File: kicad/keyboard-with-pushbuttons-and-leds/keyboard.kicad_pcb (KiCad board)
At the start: 2 copper layers, 138 parts, among them J1 CONN_01X02_MALE, J2 CONN_01X02_MALE, J3 CONN_01X04_MALE, J4 CONN_02X20, SW1 SW_Push, SW10 SW_Push, SW11 SW_Push, SW12 SW_Push, SW13 SW_Push, SW14 SW_Push, SW15 SW_Push, SW16 SW_Push, SW17 SW_Push, SW18 SW_Push, SW19 SW_Push, SW2 SW_Push, SW20 SW_Push, SW21 SW_Push, SW22 SW_Push, SW23 SW_Push, SW24 SW_Push, SW25 SW_Push, SW26 SW_Push, SW27 SW_Push, SW28 SW_Push, SW29 SW_Push, SW3 SW_Push, SW30 SW_Push, SW31 SW_Push, SW32 SW_Push, SW33 SW_Push, SW34 SW_Push, SW35 SW_Push, SW36 SW_Push, SW37 SW_Push, SW38 SW_Push, SW39 SW_Push, SW4 SW_Push, SW40 SW_Push, SW41 SW_Push, SW42 SW_Push, SW43 SW_Push, SW44 SW_Push, SW5 SW_Push, SW6 SW_Push, SW7 SW_Push, SW8 SW_Push, SW9 SW_Push

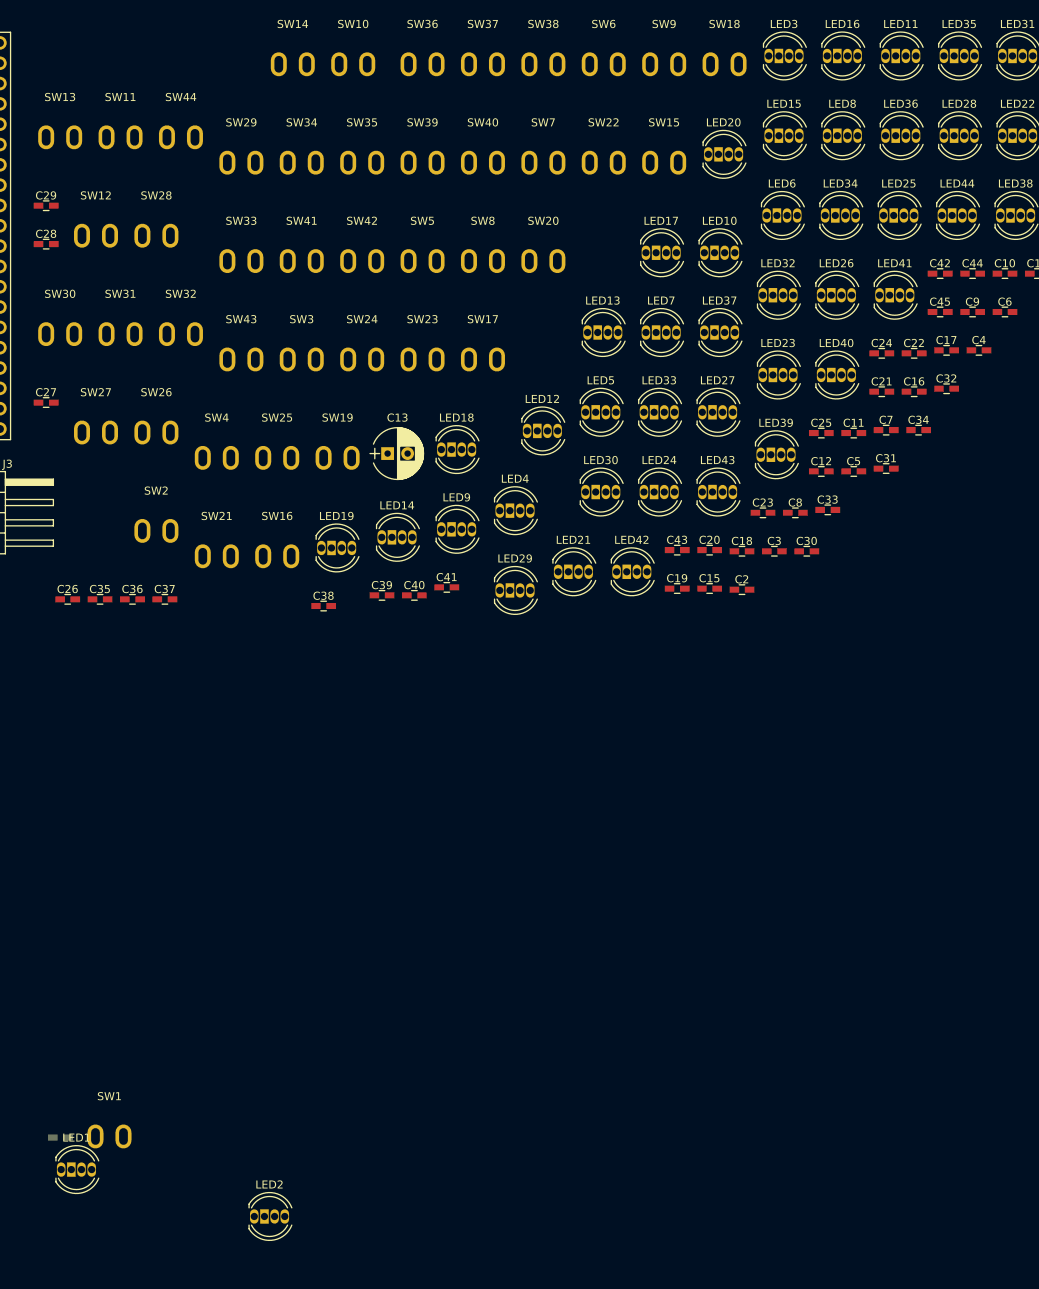
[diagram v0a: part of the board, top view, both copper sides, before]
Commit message: start creating a pattern
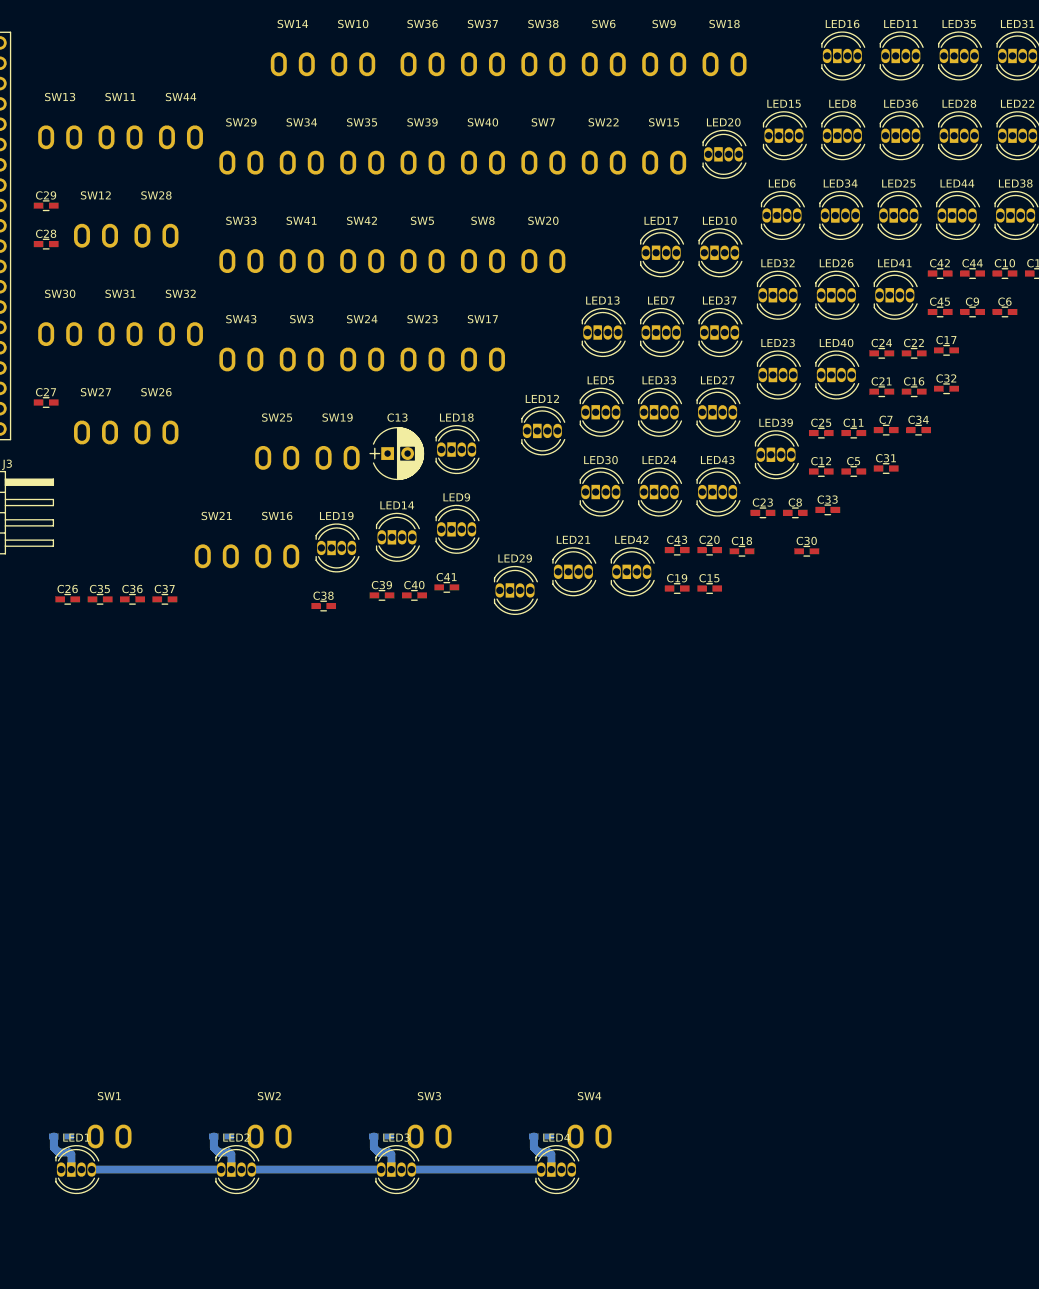
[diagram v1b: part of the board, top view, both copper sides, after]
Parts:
- added SW3: SW_Push, RedPushButton:SW_PUSH_6mm, F.Cu at (80.0, 160.0)
- C2, C3, C4: moved to B.Cu
- moved LED3 147.4 mm to (75.9, 164.1)
- moved C4 112.5 mm to (94.0, 160.0), turned to 180 degrees
- moved SW4 96.8 mm to (100.0, 160.0)
- moved C2 94.4 mm to (54.0, 160.0), turned to 180 degrees
- moved C3 88.1 mm to (74.0, 160.0), turned to 180 degrees
- moved LED4 82.5 mm to (95.9, 164.1)
- moved SW2 77.0 mm to (60.0, 160.0)
- moved LED2 7.18 mm to (55.9, 164.1)
- moved C1 0.19 mm to (34.0, 160.0)
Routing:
- net VccLed: track 0.00 -> 23.3 mm
- net Net-(LED3-Pad2): track 0.00 -> 16.2 mm
- net Net-(LED2-Pad2): track 0.00 -> 16.2 mm
- net Net-(LED1-Pad2): track 0.00 -> 16.2 mm
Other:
- net class Default: clearance 0.5 -> 0; trace_width 0.8 -> 1
- rule trace_clearance: 0.5 -> 0

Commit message: keyboard pcb: two lines
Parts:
- removed the C10 at (151.9, 52.1)
- removed the C11 at (133.0, 72.1)
- removed the C12 at (129.0, 76.9)
- removed the C14 at (156.0, 52.1)
- removed the C15 at (115.0, 91.5)
- removed the C16 at (140.6, 66.9)
- removed the C17 at (144.6, 61.7)
- removed the C18 at (119.1, 86.8)
- removed the C19 at (111.0, 91.5)
- removed the C20 at (115.0, 86.7)
- removed the C21 at (136.5, 66.9)
- removed the C22 at (140.6, 62.1)
- removed the C23 at (121.7, 82.0)
- removed the C24 at (136.5, 62.1)
- removed the C25 at (129.0, 72.1)
- removed the C6 at (151.9, 56.9)
- removed the C7 at (137.1, 71.7)
- removed the C8 at (125.7, 82.0)
- removed the C9 at (147.9, 56.9)
- removed J3: CONN_01X04_MALE, Pin_Headers:Pin_Header_Angled_1x04_Pitch2.54mm
- removed J4: CONN_02X20, Pin_Headers:Pin_Header_Straight_2x20_Pitch2.54mm
- removed the LED13 at (101.7, 59.5)
- removed the LED14 at (75.9, 85.1)
- removed the LED15 at (124.3, 34.9)
- removed the LED16 at (131.6, 24.9)
- removed the LED17 at (109.0, 49.5)
- removed the LED18 at (83.4, 74.1)
- removed the LED19 at (68.4, 86.4)
- removed the LED20 at (116.8, 37.2)
- removed the LED21 at (98.0, 89.4)
- removed the LED22 at (153.5, 34.9)
- removed the LED23 at (123.6, 64.8)
- removed the LED24 at (108.7, 79.4)
- removed the LED25 at (138.7, 44.9)
- removed the SW13 at (33.8, 35.1)
- removed the SW14 at (62.9, 26.0)
- removed the SW15 at (109.3, 38.3)
- removed the SW16 at (61.0, 87.5)
- removed the SW17 at (86.7, 62.9)
- removed the SW18 at (116.9, 26.0)
- removed the SW19 at (68.5, 75.2)
- removed the SW20 at (94.2, 50.6)
- removed the SW21 at (53.4, 87.5)
- removed the SW22 at (101.8, 38.3)
- removed the SW23 at (79.1, 62.9)
- removed the SW24 at (71.6, 62.9)
- removed the SW25 at (61.0, 75.2)
- removed the SW3 at (64.0, 62.9)
- added C10: C, Capacitors_SMD:C_0603_HandSoldering, B.Cu at (214.0, 160.0)
- added C10, C11, C12, C14, C15, C16, C17, C18, C19, C20, C21, C22, C23, C24, C25, C6, C7, C8, C9: C, Capacitors_SMD:C_0603_HandSoldering, F.Cu at (0.00, 0.00)
- added C11: C, Capacitors_SMD:C_0603_HandSoldering, B.Cu at (234.0, 160.0)
- added C12: C, Capacitors_SMD:C_0603_HandSoldering, B.Cu at (254.0, 160.0)
- added C13: C, Capacitors_SMD:C_0603_HandSoldering, B.Cu at (24.0, 142.7)
- added C14: C, Capacitors_SMD:C_0603_HandSoldering, B.Cu at (44.0, 142.7)
- added C15: C, Capacitors_SMD:C_0603_HandSoldering, B.Cu at (64.0, 142.7)
- added C16: C, Capacitors_SMD:C_0603_HandSoldering, B.Cu at (84.0, 142.7)
- added C17: C, Capacitors_SMD:C_0603_HandSoldering, B.Cu at (104.0, 142.7)
- added C18: C, Capacitors_SMD:C_0603_HandSoldering, B.Cu at (124.0, 142.7)
- added C19: C, Capacitors_SMD:C_0603_HandSoldering, B.Cu at (144.0, 142.7)
- added C20: C, Capacitors_SMD:C_0603_HandSoldering, B.Cu at (164.0, 142.7)
- added C21: C, Capacitors_SMD:C_0603_HandSoldering, B.Cu at (184.0, 142.7)
- added C22: C, Capacitors_SMD:C_0603_HandSoldering, B.Cu at (204.0, 142.7)
- added C23: C, Capacitors_SMD:C_0603_HandSoldering, B.Cu at (224.0, 142.7)
- added C24: C, Capacitors_SMD:C_0603_HandSoldering, B.Cu at (244.0, 142.7)
- added C25: C, Capacitors_SMD:C_0603_HandSoldering, B.Cu at (264.0, 142.7)
- added C6: C, Capacitors_SMD:C_0603_HandSoldering, B.Cu at (134.0, 160.0)
- added C7: C, Capacitors_SMD:C_0603_HandSoldering, B.Cu at (154.0, 160.0)
- added C8: C, Capacitors_SMD:C_0603_HandSoldering, B.Cu at (174.0, 160.0)
- added C9: C, Capacitors_SMD:C_0603_HandSoldering, B.Cu at (194.0, 160.0)
- added LED13: WS2812B, WS2812B-5mm-1:LED_D5.0mm-4, F.Cu at (25.9, 146.8)
- added LED13, LED14, LED15, LED16, LED17, LED18, LED19, LED20, LED21, LED22, LED23, LED24, LED25: WS2812B, WS2812B-5mm-1:LED_D5.0mm-4, F.Cu at (0.00, 0.00)
- added LED14: WS2812B, WS2812B-5mm-1:LED_D5.0mm-4, F.Cu at (45.9, 146.8)
- added LED15: WS2812B, WS2812B-5mm-1:LED_D5.0mm-4, F.Cu at (65.9, 146.8)
- added LED16: WS2812B, WS2812B-5mm-1:LED_D5.0mm-4, F.Cu at (85.9, 146.8)
- added LED17: WS2812B, WS2812B-5mm-1:LED_D5.0mm-4, F.Cu at (105.9, 146.8)
- added LED18: WS2812B, WS2812B-5mm-1:LED_D5.0mm-4, F.Cu at (125.9, 146.8)
- added LED19: WS2812B, WS2812B-5mm-1:LED_D5.0mm-4, F.Cu at (145.9, 146.8)
- added LED20: WS2812B, WS2812B-5mm-1:LED_D5.0mm-4, F.Cu at (165.9, 146.8)
- added LED21: WS2812B, WS2812B-5mm-1:LED_D5.0mm-4, F.Cu at (185.9, 146.8)
- added LED22: WS2812B, WS2812B-5mm-1:LED_D5.0mm-4, F.Cu at (205.9, 146.8)
- added LED23: WS2812B, WS2812B-5mm-1:LED_D5.0mm-4, F.Cu at (225.9, 146.8)
- added LED24: WS2812B, WS2812B-5mm-1:LED_D5.0mm-4, F.Cu at (245.9, 146.8)
- added LED25: WS2812B, WS2812B-5mm-1:LED_D5.0mm-4, F.Cu at (265.9, 146.8)
- added SW13: SW_Push, RedPushButton:SW_PUSH_6mm, F.Cu at (30.0, 142.7)
- added SW13, SW14, SW15, SW16, SW17, SW18, SW19, SW20, SW21, SW22, SW23, SW24, SW25: SW_Push, RedPushButton:SW_PUSH_6mm, F.Cu at (0.00, 0.00)
- added SW14: SW_Push, RedPushButton:SW_PUSH_6mm, F.Cu at (50.0, 142.7)
- added SW15: SW_Push, RedPushButton:SW_PUSH_6mm, F.Cu at (70.0, 142.7)
- added SW16: SW_Push, RedPushButton:SW_PUSH_6mm, F.Cu at (90.0, 142.7)
- added SW17: SW_Push, RedPushButton:SW_PUSH_6mm, F.Cu at (110.0, 142.7)
- added SW18: SW_Push, RedPushButton:SW_PUSH_6mm, F.Cu at (130.0, 142.7)
- added SW19: SW_Push, RedPushButton:SW_PUSH_6mm, F.Cu at (150.0, 142.7)
- added SW20: SW_Push, RedPushButton:SW_PUSH_6mm, F.Cu at (170.0, 142.7)
- added SW21: SW_Push, RedPushButton:SW_PUSH_6mm, F.Cu at (190.0, 142.7)
- added SW22: SW_Push, RedPushButton:SW_PUSH_6mm, F.Cu at (210.0, 142.7)
- added SW23: SW_Push, RedPushButton:SW_PUSH_6mm, F.Cu at (230.0, 142.7)
- added SW24: SW_Push, RedPushButton:SW_PUSH_6mm, F.Cu at (250.0, 142.7)
- added SW25: SW_Push, RedPushButton:SW_PUSH_6mm, F.Cu at (270.0, 142.7)
- C45: value C -> 1000uF
- C5: moved to B.Cu
- moved SW12 248.6 mm to (260.0, 160.0)
- moved SW11 234.6 mm to (240.0, 160.0)
- moved SW10 200.8 mm to (220.0, 160.0)
- moved LED12 186.3 mm to (255.9, 164.1)
- moved LED11 169.6 mm to (235.9, 164.1)
- moved SW9 161.8 mm to (200.0, 160.0)
- moved LED38 159.7 mm to (0.00, 0.00)
- moved C32 159.2 mm to (0.00, 0.00)
- moved C34 158.3 mm to (0.00, 0.00)
- moved C31 157.0 mm to (0.00, 0.00)
- moved C44 156.8 mm to (0.00, 0.00)
- moved LED31 155.5 mm to (0.00, 0.00)
- moved C45 154.7 mm to (0.00, 0.00)
- moved C30 154.0 mm to (0.00, 0.00)
- moved C33 153.3 mm to (0.00, 0.00)
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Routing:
- net VccLed: track 23.3 -> 674.7 mm
- net Net-(LED12-Pad2): track 0.00 -> 262.6 mm
- net Net-(LED24-Pad2): track 0.00 -> 16.2 mm
- net Net-(LED8-Pad2): track 0.00 -> 16.2 mm
- net Net-(LED7-Pad2): track 0.00 -> 16.2 mm
- net Net-(LED6-Pad2): track 0.00 -> 16.2 mm
- net Net-(LED5-Pad2): track 0.00 -> 16.2 mm
- net Net-(LED4-Pad2): track 0.00 -> 16.2 mm
- net Net-(LED23-Pad2): track 0.00 -> 16.2 mm
- net Net-(LED22-Pad2): track 0.00 -> 16.2 mm
- net Net-(LED21-Pad2): track 0.00 -> 16.2 mm
- net Net-(LED20-Pad2): track 0.00 -> 16.2 mm
- net Net-(LED19-Pad2): track 0.00 -> 16.2 mm
- net Net-(LED18-Pad2): track 0.00 -> 16.2 mm
- net Net-(LED17-Pad2): track 0.00 -> 16.2 mm
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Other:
- net class Default: clearance 0 -> 0.1
- rule trace_clearance: 0 -> 0.1

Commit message: full board for keyboard
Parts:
- removed the C10 at (0.00, 0.00)
- removed the C11 at (0.00, 0.00)
- removed the C12 at (0.00, 0.00)
- removed the C14 at (0.00, 0.00)
- removed the C15 at (0.00, 0.00)
- removed the C16 at (0.00, 0.00)
- removed the C17 at (0.00, 0.00)
- removed the C18 at (0.00, 0.00)
- removed the C19 at (0.00, 0.00)
- removed the C20 at (0.00, 0.00)
- removed the C21 at (0.00, 0.00)
- removed the C22 at (0.00, 0.00)
- removed the C23 at (0.00, 0.00)
- removed the C24 at (0.00, 0.00)
- removed the C25 at (0.00, 0.00)
- removed the C45 at (0.00, 0.00)
- removed the C6 at (0.00, 0.00)
- removed the C7 at (0.00, 0.00)
- removed the C8 at (0.00, 0.00)
- removed the C9 at (0.00, 0.00)
- removed the LED13 at (0.00, 0.00)
- removed the LED14 at (0.00, 0.00)
- removed the LED15 at (0.00, 0.00)
- removed the LED16 at (0.00, 0.00)
- removed the LED17 at (0.00, 0.00)
- removed the LED18 at (0.00, 0.00)
- removed the LED19 at (0.00, 0.00)
- removed the LED20 at (0.00, 0.00)
- removed the LED21 at (0.00, 0.00)
- removed the LED22 at (0.00, 0.00)
- removed the LED23 at (0.00, 0.00)
- removed the LED24 at (0.00, 0.00)
- removed the LED25 at (0.00, 0.00)
- removed the SW13 at (0.00, 0.00)
- removed the SW14 at (0.00, 0.00)
- removed the SW15 at (0.00, 0.00)
- removed the SW16 at (0.00, 0.00)
- removed the SW17 at (0.00, 0.00)
- removed the SW18 at (0.00, 0.00)
- removed the SW19 at (0.00, 0.00)
- removed the SW20 at (0.00, 0.00)
- removed the SW21 at (0.00, 0.00)
- removed the SW22 at (0.00, 0.00)
- removed the SW23 at (0.00, 0.00)
- removed the SW24 at (0.00, 0.00)
- removed the SW25 at (0.00, 0.00)
- C26, C27, C28, C29, C30, C31, C32, C33, C34, C35, C36, C37, C38, C39, C40, C41, C42, C43, C44: moved to B.Cu
- moved SW37 288.6 mm to (260.0, 125.4)
- moved LED37 286.8 mm to (255.9, 129.5)
- moved C37 283.3 mm to (254.0, 125.4), turned to 180 degrees
- moved SW36 270.8 mm to (240.0, 125.4)
- moved LED36 269.1 mm to (235.9, 129.5)
- moved C36 265.5 mm to (234.0, 125.4), turned to 180 degrees
- moved SW35 253.2 mm to (220.0, 125.4)
- moved LED35 251.7 mm to (215.9, 129.5)
- moved C35 248.0 mm to (214.0, 125.4), turned to 180 degrees
- moved SW34 236.0 mm to (200.0, 125.4)
- moved LED34 234.8 mm to (195.9, 129.5)
- moved C34 231.0 mm to (194.0, 125.4), turned to 180 degrees
- moved SW33 219.4 mm to (180.0, 125.4)
- moved SW44 218.6 mm to (190.0, 108.0)
- moved LED33 218.4 mm to (175.9, 129.5)
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- renumbered C13 to C45
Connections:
- LED25 pad 2: Net-(LED24-Pad2) -> Net-(LED25-Pad2)
- LED25 pad 4: Net-(LED23-Pad2) -> Net-(LED24-Pad2)
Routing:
- net VccLed: track 674.7 -> 1296.5 mm
- net Net-(LED25-Pad2): track 0.00 -> 262.7 mm
- net Net-(LED37-Pad2): track 0.00 -> 223.5 mm
- net Net-(LED1-Pad4): track 0.00 -> 50.7 mm
- net Net-(LED43-Pad2): track 0.00 -> 16.2 mm
- net Net-(LED42-Pad2): track 0.00 -> 16.2 mm
- net Net-(LED41-Pad2): track 0.00 -> 16.2 mm
- net Net-(LED40-Pad2): track 0.00 -> 16.2 mm
- net Net-(LED39-Pad2): track 0.00 -> 16.2 mm
- net Net-(LED38-Pad2): track 0.00 -> 16.2 mm
- net Net-(LED36-Pad2): track 0.00 -> 16.2 mm
- net Net-(LED35-Pad2): track 0.00 -> 16.2 mm
- net Net-(LED34-Pad2): track 0.00 -> 16.2 mm
- net Net-(LED33-Pad2): track 0.00 -> 16.2 mm
- net Net-(LED32-Pad2): track 0.00 -> 16.2 mm
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- added copper zone on B.Cu, net GND
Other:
- board outline added: 290 x 80 mm
- net class Default: clearance 0.1 -> 0.5
- rule trace_clearance: 0.1 -> 0.5
